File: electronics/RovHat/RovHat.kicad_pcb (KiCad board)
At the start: 4 copper layers, 85 x 56 mm, 34 parts, among them J201 Conn_01x10, J301 PICO_1-20, J302 PICO_SWD, J303 Conn_01x02, J304 PICO_21-40, J305 SWD_EXT, J401 Conn_02x20_Odd_Even, J402 USB_A, U301 W25Q128JVS, U302 ASDMB-xxxMHz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

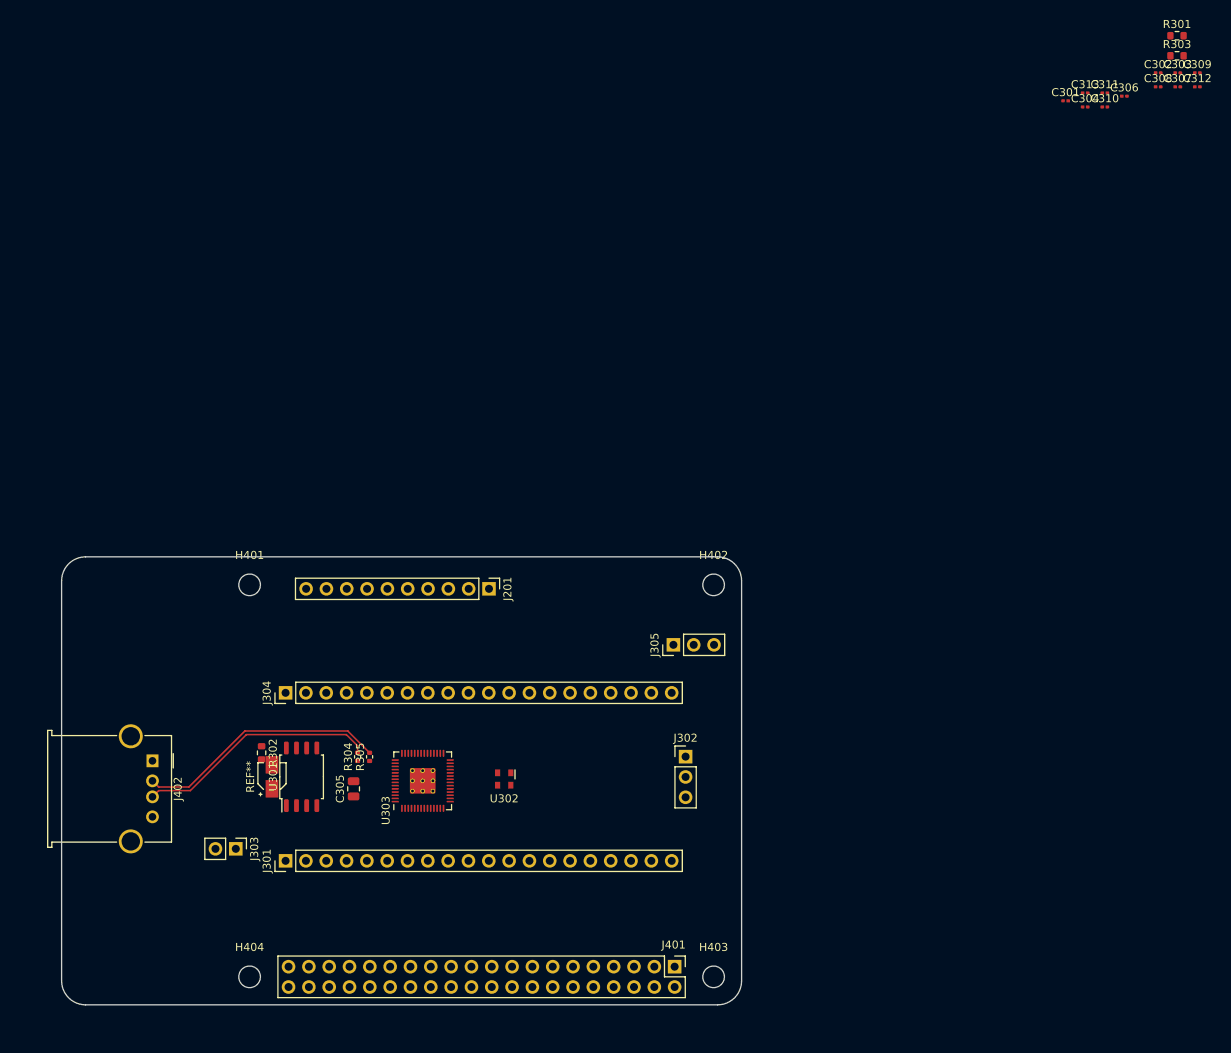
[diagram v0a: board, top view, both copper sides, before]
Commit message: Changed To RPI Pico Module
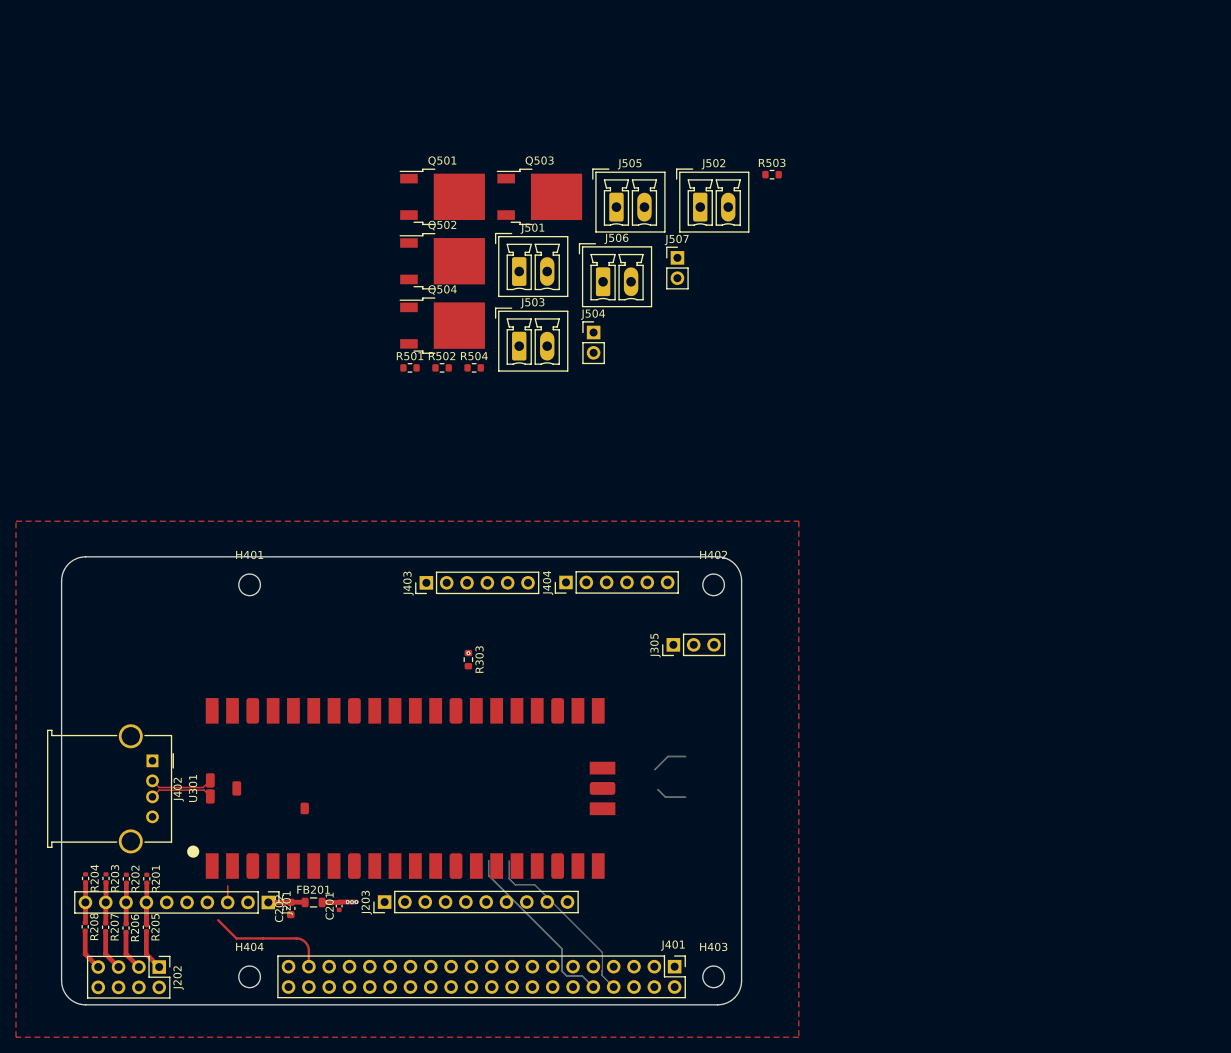
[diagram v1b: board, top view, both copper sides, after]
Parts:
- removed C301, C302, C303, C304, C306, C307, C308, C309, C310, C311, C312, C313: 100n, Capacitor_SMD:C_0201_0603Metric
- removed C305: 1u, Capacitor_SMD:C_0805_2012Metric
- removed J301: PICO_1-20, Connector_PinHeader_2.54mm:PinHeader_1x20_P2.54mm_Vertical
- removed J302: PICO_SWD, Connector_PinHeader_2.54mm:PinHeader_1x03_P2.54mm_Vertical
- removed J303: Conn_01x02, Connector_PinHeader_2.54mm:PinHeader_1x02_P2.54mm_Vertical
- removed J304: PICO_21-40, Connector_PinHeader_2.54mm:PinHeader_1x20_P2.54mm_Vertical
- removed R301: 1k, Resistor_SMD:R_0603_1608Metric
- removed R302: 10k, Resistor_SMD:R_0603_1608Metric
- removed R304, R305: 27, Resistor_SMD:R_0402_1005Metric
- removed REF**: CP_Elec_3x5.3, Capacitor_SMD:CP_Elec_3x5.3
- removed U302: ASDMB-xxxMHz, Oscillator:Oscillator_SMD_Abracon_ASDMB-4Pin_2.5x2.0mm
- removed U303: RP2040, Findersee_parts:RP2040-QFN-56
- added C201: 1u, Capacitor_SMD:C_0402_1005Metric, F.Cu at (102.2, 135.2)
- added C202: 1u, Capacitor_SMD:C_0603_1608Metric, F.Cu at (96.2, 135.4)
- added FB201: 600R@100M, Inductor_SMD:L_0805_2012Metric, F.Cu at (99.0, 134.7)
- added J202: Conn_02x04_Odd_Even, Connector_PinHeader_2.54mm:PinHeader_2x04_P2.54mm_Vertical, F.Cu at (79.7, 142.8)
- added J203: Conn_01x10, Connector_PinHeader_2.54mm:PinHeader_1x10_P2.54mm_Vertical, F.Cu at (107.9, 134.7)
- added J403: DEPTH, Connector_PinHeader_2.54mm:PinHeader_1x06_P2.54mm_Vertical, F.Cu at (113.1, 94.8)
- added J404: PROPULSION, Connector_PinHeader_2.54mm:PinHeader_1x06_P2.54mm_Vertical, F.Cu at (130.6, 94.7)
- added J501: OUT1, Connector_Phoenix_MC:PhoenixContact_MCV_1,5_2-G-3.5_1x02_P3.50mm_Vertical, F.Cu at (124.7, 55.8)
- added J502: OUT2, Connector_Phoenix_MC:PhoenixContact_MCV_1,5_2-G-3.5_1x02_P3.50mm_Vertical, F.Cu at (147.3, 47.8)
- added J503: OUT3, Connector_Phoenix_MC:PhoenixContact_MCV_1,5_2-G-3.5_1x02_P3.50mm_Vertical, F.Cu at (124.7, 65.2)
- added J504: 5V IN, Connector_PinHeader_2.54mm:PinHeader_1x02_P2.54mm_Vertical, F.Cu at (134.0, 63.5)
- added J505: OUT4, Connector_Phoenix_MC:PhoenixContact_MCV_1,5_2-G-3.5_1x02_P3.50mm_Vertical, F.Cu at (136.9, 47.8)
- added J506: PWR IN, Connector_Phoenix_MC:PhoenixContact_MCV_1,5_2-G-3.5_1x02_P3.50mm_Vertical, F.Cu at (135.2, 57.1)
- added J507: PWR OUT, Connector_PinHeader_2.54mm:PinHeader_1x02_P2.54mm_Vertical, F.Cu at (144.5, 54.1)
- added Q501: AOD508, Package_TO_SOT_SMD:TO-252-2, F.Cu at (115.1, 46.5)
- added Q502: AOD508, Package_TO_SOT_SMD:TO-252-2, F.Cu at (115.1, 54.5)
- added Q503: AOD508, Package_TO_SOT_SMD:TO-252-2, F.Cu at (127.3, 46.5)
- added Q504: AOD508, Package_TO_SOT_SMD:TO-252-2, F.Cu at (115.1, 62.6)
- added R201: 20k, Resistor_SMD:R_0402_1005Metric, F.Cu at (78.2, 131.8)
- added R202: 20k, Resistor_SMD:R_0402_1005Metric, F.Cu at (75.6, 131.8)
- added R203: 20k, Resistor_SMD:R_0402_1005Metric, F.Cu at (73.0, 131.7)
- added R204: 20k, Resistor_SMD:R_0402_1005Metric, F.Cu at (70.5, 131.7)
- added R205: 10k, Resistor_SMD:R_0402_1005Metric, F.Cu at (78.1, 137.8)
- added R206: 10k, Resistor_SMD:R_0402_1005Metric, F.Cu at (75.5, 137.9)
- added R207: 10k, Resistor_SMD:R_0402_1005Metric, F.Cu at (73.0, 137.8)
- added R208: 10k, Resistor_SMD:R_0402_1005Metric, F.Cu at (70.5, 137.8)
- added R501: R_Small, Resistor_SMD:R_0603_1608Metric, F.Cu at (111.0, 67.9)
- added R502: R_Small, Resistor_SMD:R_0603_1608Metric, F.Cu at (115.1, 67.9)
- added R503: R_Small, Resistor_SMD:R_0603_1608Metric, F.Cu at (156.3, 43.7)
- added R504: R_Small, Resistor_SMD:R_0603_1608Metric, F.Cu at (119.1, 67.9)
- U301: value W25Q128JVS -> Rpi_Pico; footprint Package_SO:SOIC-8_5.23x5.23mm_P1.27mm -> Findersee_parts:RP_PICO
- moved R303 116.4 mm to (118.3, 104.3), turned to -90 degrees
- moved J201 47.9 mm to (93.3, 134.7)
- moved U301 13.0 mm to (110.5, 120.5), turned to 0 degrees
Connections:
- J201 pad 3: /MCU/SCL -> /Sensors/SCL
- J201 pad 4: /MCU/SDA -> /Sensors/SDA
- J401 pad 10: /MCU/TX -> /Connectors/RPI_RXD
- J401 pad 16: /Connectors/BOOT_SEL -> unconnected-(J401-Pad16)
- J401 pad 18: /MCU/RUN -> /Connectors/RESET
- J401 pad 37: unconnected-(J401-Pad37) -> /Connectors/BOOT_SEL
- J401 pad 8: /MCU/RX -> /Connectors/RPI_TXD
- R303 pad 2: /MCU/RUN -> /Connectors/RESET
- U301 pad 1: /MCU/SS -> /MCU/SDA
- U301 pad 2: /MCU/SD1 -> /MCU/SCL
- U301 pad 3: /MCU/SD2 -> GND
- U301 pad 4: GND -> /MCU/PWM1
- U301 pad 5: /MCU/SD0 -> /MCU/PWM2
- U301 pad 6: /MCU/SCLK -> /MCU/PWM3
- U301 pad 7: /MCU/SD3 -> /MCU/PWM4
- U301 pad 8: VDD -> GND
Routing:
- net /Connectors/USB -: track 31.5 -> 7.94 mm
- net /Connectors/RPI_TXD: track 0.00 -> 22.7 mm
- net /Connectors/USB +: track 30.3 -> 7.90 mm
- net /Connectors/RPI_RXD: track 0.00 -> 22.4 mm
- net /Connectors/BOOT_SEL: track 0.00 -> 15.1 mm
- net /Sensors/A0: track 0.00 -> 7.86 mm
- net Net-(J202-Pad7): track 0.00 -> 5.19 mm
- net /Sensors/A1: track 0.00 -> 5.15 mm
- net Net-(J202-Pad5): track 0.00 -> 5.14 mm
- net Net-(J202-Pad1): track 0.00 -> 5.13 mm
- net /Sensors/A2: track 0.00 -> 5.10 mm
- net /Sensors/A3: track 0.00 -> 5.05 mm
- net Net-(J202-Pad3): track 0.00 -> 5.03 mm
- net +3.3VA: track 0.00 -> 4.61 mm
- net /MCU/SWDIO: track 0.00 -> 4.53 mm
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- added copper zone on F.Cu, net GND
- added copper zone on In1.Cu, net GND
- added copper zone on In2.Cu, net VDD

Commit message: Layout Done first level
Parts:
- J401: value Conn_02x20_Odd_Even -> RPI Header
- Q501, Q502, Q503, Q504: value AOD508 -> IRF7403; footprint Package_TO_SOT_SMD:TO-252-2 -> Package_SO:SOIC-8_3.9x4.9mm_P1.27mm
- moved J504 74.9 mm to (144.1, 137.7), turned to -90 degrees
- moved R503 66.7 mm to (134.0, 106.6), turned to 90 degrees
- moved J507 60.1 mm to (99.7, 94.2)
- moved J404 59.4 mm to (71.2, 97.0)
- moved Q503 58.6 mm to (130.4, 105.0), turned to 90 degrees
- moved Q501 58.5 mm to (115.6, 105.0), turned to 90 degrees
- moved J502 52.7 mm to (123.1, 94.6), turned to -90 degrees
- moved Q502 51.1 mm to (123.0, 105.0), turned to 90 degrees
- moved Q504 48.1 mm to (137.8, 105.0), turned to 90 degrees
- moved J506 47.7 mm to (105.7, 94.6), turned to -90 degrees
- moved J505 47.0 mm to (140.5, 94.6), turned to -90 degrees
- moved R504 44.7 mm to (141.4, 106.7), turned to 90 degrees
- moved J403 43.0 mm to (71.2, 104.2)
- moved J203 42.7 mm to (150.6, 132.2), turned to 180 degrees
- moved R502 40.5 mm to (126.7, 106.6), turned to 90 degrees
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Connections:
- J203 pad 10: /Sensors/LSM_DRDY -> /MCU/LSM_DRDY
- J203 pad 6: /Sensors/GYRO_INT -> /MCU/GYRO_INT
- J203 pad 7: /Sensors/GYRO_RDY -> /MCU/GYRO_RDY
- J203 pad 8: /Sensors/LSM_INT1 -> /MCU/LSM_INT1
- J203 pad 9: /Sensors/LSM_INT2 -> /MCU/LSM_INT2
- J402 pad 1: +5V -> VBUS
- Q501 pad 1: /Power + FETs/CH1 -> GND
- Q501 pad 2: Net-(J501-Pad2) -> GND
- Q502 pad 1: /Power + FETs/CH2 -> GND
- Q502 pad 2: Net-(J502-Pad2) -> GND
- Q503 pad 1: /Power + FETs/CH3 -> GND
- Q503 pad 2: Net-(J503-Pad2) -> GND
- Q504 pad 1: /Power + FETs/CH4 -> GND
- Q504 pad 2: Net-(J505-Pad2) -> GND
- R501 pad 1: /Power + FETs/CH1 -> /MCU/PWM_1
- R502 pad 1: /Power + FETs/CH2 -> /MCU/PWM_2
- R503 pad 1: /Power + FETs/CH3 -> /MCU/PWM_3
- R504 pad 1: /Power + FETs/CH4 -> /MCU/PWM_4
- U301 pad 1: /MCU/SDA -> /Sensors/SDA
- U301 pad 11: /MCU/TX -> /Connectors/RPI_RXD
- U301 pad 12: /MCU/RX -> /Connectors/RPI_TXD
- U301 pad 14: unconnected-(U301-Pad14) -> /MCU/LSM_DRDY
- U301 pad 15: unconnected-(U301-Pad15) -> /MCU/LSM_INT2
- U301 pad 16: unconnected-(U301-Pad16) -> /MCU/LSM_INT1
- U301 pad 17: unconnected-(U301-Pad17) -> /MCU/GYRO_RDY
- U301 pad 19: unconnected-(U301-Pad19) -> /MCU/GYRO_INT
- U301 pad 2: /MCU/SCL -> /Sensors/SCL
- U301 pad 21: unconnected-(U301-Pad21) -> /MCU/PWM_4
- U301 pad 22: unconnected-(U301-Pad22) -> /MCU/PWM_3
- U301 pad 24: /MCU/PIO4 -> /MCU/PWM_2
- U301 pad 25: /MCU/PIO3 -> /MCU/PWM_1
- U301 pad 26: /MCU/PIO2 -> unconnected-(U301-Pad26)
- U301 pad 27: /MCU/PIO1 -> unconnected-(U301-Pad27)
- U301 pad 29: unconnected-(U301-Pad29) -> /Connectors/PR
- U301 pad 31: unconnected-(U301-Pad31) -> /Connectors/PL
- U301 pad 32: unconnected-(U301-Pad32) -> /Connectors/DR
- U301 pad 34: unconnected-(U301-Pad34) -> /Connectors/DL
- U301 pad 4: /MCU/PWM1 -> unconnected-(U301-Pad4)
- U301 pad 40: unconnected-(U301-Pad40) -> VBUS
- U301 pad 5: /MCU/PWM2 -> unconnected-(U301-Pad5)
- U301 pad 6: /MCU/PWM3 -> unconnected-(U301-Pad6)
- U301 pad 7: /MCU/PWM4 -> unconnected-(U301-Pad7)
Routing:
- net /Sensors/SDA: track 0.00 -> 81.6 mm
- net /Sensors/SCL: track 2.07 -> 71.5 mm, vias 0 -> 1
- net VDD: track 4.33 -> 61.6 mm, vias 4 -> 17
- net /Connectors/PR: track 0.00 -> 56.9 mm
- net /Connectors/RESET: track 0.00 -> 51.1 mm, vias 0 -> 1
- net /Connectors/PL: track 0.00 -> 48.5 mm
- net /MCU/LSM_DRDY: track 0.00 -> 46.0 mm, vias 0 -> 1
- net /MCU/LSM_INT2: track 0.00 -> 42.2 mm, vias 0 -> 1
- net /MCU/LSM_INT1: track 0.00 -> 38.2 mm, vias 0 -> 1
- net /Connectors/DL: track 0.00 -> 37.2 mm
- net /MCU/GYRO_RDY: track 0.00 -> 34.4 mm, vias 0 -> 1
- net /Connectors/DR: track 0.00 -> 33.9 mm
- net /Connectors/BOOT_SEL: track 15.1 -> 47.9 mm
- net /MCU/GYRO_INT: track 0.00 -> 32.3 mm, vias 0 -> 1
- net /Connectors/RPI_TXD: track 22.7 -> 35.5 mm
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- added copper zone on In2.Cu, net +5V
- added copper zone on F.Cu, net +VSW
- added copper zone on B.Cu, net GND
- added copper zone on F.Cu, net Net-(J501-Pad2)
- added copper zone on F.Cu, net Net-(J502-Pad2)
- added copper zone on F.Cu, net Net-(J503-Pad2)
- added copper zone on F.Cu, net Net-(J505-Pad2)
- added copper zone on B.Cu, net VDD
- added copper zone on F.Cu, net VDD
- removed copper zone on In2.Cu, net VDD

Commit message: Fabrication commit
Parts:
- removed C201: 1u, Capacitor_SMD:C_0402_1005Metric
- removed C202: 1u, Capacitor_SMD:C_0603_1608Metric
- removed FB201: 600R@100M, Inductor_SMD:L_0805_2012Metric
- added J301: PWM_OUT, Connector_PinHeader_2.54mm:PinHeader_1x03_P2.54mm_Vertical, F.Cu at (104.1, 135.8)
- added J508: PWR OUT2, Connector_Phoenix_MC:PhoenixContact_MCV_1,5_2-G-3.5_1x02_P3.50mm_Vertical, F.Cu at (97.6, 94.6)
- added R209: 4k7, Resistor_SMD:R_0603_1608Metric, F.Cu at (87.2, 139.8)
- added R210: 4k7, Resistor_SMD:R_0603_1608Metric, F.Cu at (141.5, 129.3)
- added R211: 4k7, Resistor_SMD:R_0603_1608Metric, F.Cu at (139.6, 129.3)
- added REF**: Logo, Findersee_parts:Logo, B.Cu at (69.9, 120.3)
- added REF**: KiCad-Logo2_8mm_SilkScreen, Symbol:KiCad-Logo2_8mm_SilkScreen, B.Cu at (100.4, 103.4)
- J201: value Conn_01x10 -> ADS1115
- J202: value Conn_02x04_Odd_Even -> ANALOG INPUT
- J203: value Conn_01x10 -> GYRO
- R201, R202, R203, R204, R205, R206, R207, R208: footprint Resistor_SMD:R_0402_1005Metric -> Resistor_SMD:R_0603_1608Metric
- moved J507 47.9 mm to (147.2, 99.9)
- moved R303 2.40 mm to (111.7, 109.2)
- moved R201 0.70 mm to (78.1, 132.9)
- moved R202 0.70 mm to (75.6, 132.9)
- moved R203 0.70 mm to (73.0, 132.9)
- moved R204 0.70 mm to (70.5, 132.9)
- moved J202 0.40 mm to (78.1, 143.2)
- moved J201 0.20 mm to (93.3, 136.4)
- moved J506 0.20 mm to (105.9, 94.6)
- moved R205 0.10 mm to (78.1, 139.8)
- moved R206 0.10 mm to (75.6, 139.8)
- moved R207 0.10 mm to (73.0, 139.8)
- moved R208 0.10 mm to (70.5, 139.8)
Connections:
- J201 pad 1: +3.3VA -> VDD
- J201 pad 5: unconnected-(J201-Pad5) -> Net-(J201-Pad5)
- J201 pad 6: unconnected-(J201-Pad6) -> /MCU/ADS_RDY
- J203 pad 1: unconnected-(J203-Pad1) -> +5V
- U301 pad 10: unconnected-(U301-Pad10) -> Net-(U301-Pad10)
- U301 pad 27: unconnected-(U301-Pad27) -> /MCU/ADS_RDY
- U301 pad 9: unconnected-(U301-Pad9) -> Net-(U301-Pad9)
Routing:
- net /MCU/ADS_RDY: track 0.00 -> 54.0 mm
- net /Connectors/BOOT_SEL: track 47.9 -> 18.2 mm, vias 0 -> 2
- net Net-(J201-Pad5): track 0.00 -> 9.58 mm
- net VDD: track 61.6 -> 69.6 mm, vias 17 -> 16
- net +3.3VA: track 4.61 -> 0.00 mm
- net Net-(U301-Pad9): track 0.00 -> 3.72 mm
- net Net-(U301-Pad10): track 0.00 -> 3.72 mm
- net /Connectors/RESET: track 51.1 -> 47.4 mm
- net /Connectors/PR: track 56.9 -> 53.4 mm
- net /Sensors/SDA: track 81.6 -> 84.1 mm
- net /Sensors/SCL: track 71.5 -> 72.8 mm, vias 1 -> 2
- net /Connectors/PL: track 48.5 -> 49.6 mm
- net GND: vias 0 -> 54
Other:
- rule pad_to_mask_clearance: 0.1 -> 0
- board text added: "AIN"
- board text added: "DEPTH"
- board text added: "Findersee 03/23 REV 1"
- board text added: "LEFT"
- board text added: "PROPULSION"
- board text added: "RIGHT"
- board text added: "S + - S + -"
- board text added: "This side Toward Raspberry Pi"

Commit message: Fabrication commit 2
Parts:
- removed the REF** at (100.4, 103.4)
- added D501: MBR0550, Diode_SMD:D_SOD-123, F.Cu at (119.6, 103.7)
- added D502: MBR0550, Diode_SMD:D_SOD-123, F.Cu at (128.0, 103.7)
- added D503: MBR0550, Diode_SMD:D_SOD-123, F.Cu at (135.9, 103.7)
- added D504: MBR0550, Diode_SMD:D_SOD-123, F.Cu at (144.2, 103.7)
- moved Q504 2.69 mm to (140.3, 106.0)
- moved R504 2.69 mm to (143.9, 107.7)
- moved Q503 1.80 mm to (131.9, 106.0)
- moved R503 1.80 mm to (135.5, 107.6)
- moved Q502 1.41 mm to (124.0, 106.0)
- moved R502 1.27 mm to (127.5, 107.6)
- moved Q501 1.00 mm to (115.6, 106.0)
- moved R501 1.00 mm to (119.4, 107.7)
- moved REF** 0.11 mm to (69.8, 120.4)
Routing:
- net /MCU/GYRO_INT: track 32.2 -> 30.9 mm
- net /MCU/PWM_1: track 11.5 -> 10.3 mm
- net /MCU/PWM_4: track 11.1 -> 12.2 mm
- net /MCU/PWM_2: track 7.14 -> 6.34 mm
- net GND: vias 54 -> 53
